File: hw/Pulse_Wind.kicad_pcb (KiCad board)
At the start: 2 copper layers, 0 parts

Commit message: hw: Layout & routing
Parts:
- added C1: 100n, Capacitor_SMD:C_0402_1005Metric, F.Cu at (85.8, 83.5)
- added C2: 100n, Capacitor_SMD:C_0402_1005Metric, F.Cu at (78.2, 80.3)
- added C3: 100n, Capacitor_SMD:C_0402_1005Metric, F.Cu at (84.2, 83.1)
- added C4: 1n, Capacitor_SMD:C_0402_1005Metric, F.Cu at (82.3, 85.0)
- added C5: 4.7u, Capacitor_SMD:C_0402_1005Metric, F.Cu at (83.8, 84.5)
- added C6: 4.7u, Capacitor_SMD:C_0402_1005Metric, F.Cu at (83.7, 93.4)
- added C91: 1u, Capacitor_SMD:C_0402_1005Metric, F.Cu at (78.2, 82.6)
- added C92: 1u, Capacitor_SMD:C_0402_1005Metric, F.Cu at (76.0, 80.2)
- added D1: LED_RAGB, LED_THT:LED_D5.0mm-4_RGB, B.Cu at (74.7, 89.8)
- added J1: AudioJack4, Connector_Audio:Jack_3.5mm_KoreanHropartsElec_PJ-320D-4A_Horizontal, B.Cu at (80.0, 80.0)
- added J2: Conn_01x04, TestPoints_P2.00:TestPoints_1x04_P2.00, F.Cu at (83.0, 77.1)
- added LS1: Speaker, Pulse_footprints:Pads_P2.00, B.Cu at (83.7, 90.8)
- added R1: 470, Resistor_SMD:R_0402_1005Metric, F.Cu at (74.8, 87.7)
- added R2: 470, Resistor_SMD:R_0402_1005Metric, F.Cu at (77.3, 87.7)
- added R3: 470, Resistor_SMD:R_0402_1005Metric, F.Cu at (78.5, 87.7)
- added R4: 100k, Resistor_SMD:R_0402_1005Metric, F.Cu at (82.3, 83.1)
- added R5: 22k, Resistor_SMD:R_0402_1005Metric, F.Cu at (82.3, 84.0)
- added U1: PY32F003F18U6, Package_DFN_QFN:QFN-20-1EP_3x3mm_P0.4mm_EP1.65x1.65mm, F.Cu at (84.2, 80.4)
- added U2: SC7A20, Package_LGA:LGA-12_2x2mm_P0.5mm, F.Cu at (80.0, 80.0)
- added U3: FM8002A, Package_SO:SOP-8_3.9x4.9mm_P1.27mm, F.Cu at (83.7, 89.2)
- added U9: ME6206A33XG, Package_TO_SOT_SMD:SOT-23, F.Cu at (76.0, 82.5)
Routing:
- net +3V3: track 0.00 -> 53.2 mm, vias 0 -> 2
- net /LED_R: track 0.00 -> 11.7 mm
- net Net-(U3-VO1): track 0.00 -> 9.07 mm, vias 0 -> 1
- net /LED_G: track 0.00 -> 8.84 mm
- net /LED_B: track 0.00 -> 8.72 mm
- net /ID_IN: track 0.00 -> 7.61 mm, vias 0 -> 1
- net /SWCLK: track 0.00 -> 5.20 mm
- net /SWDIO: track 0.00 -> 4.80 mm
- net VIN: track 0.00 -> 4.66 mm, vias 0 -> 1
- net Net-(U3-+IN): track 0.00 -> 3.62 mm
- net Net-(U3--IN): track 0.00 -> 3.52 mm
- net /IMU_SDA: track 0.00 -> 2.37 mm
- net /IMU_SCK: track 0.00 -> 2.31 mm
- net /IMU_CS: track 0.00 -> 2.07 mm
- net Net-(D1-GK): track 0.00 -> 1.65 mm
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- added copper zone on B.Cu, net GND
- added copper zone on F.Cu, net GND
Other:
- board outline added: 14 x 21 mm

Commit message: hw: Tweaks in the details
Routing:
- added copper zone on F.Cu, net +3V3
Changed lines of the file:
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@@
 	)
 	(segment
-		(start 86.386 83.556)
-		(end 86.386 85.264)
-		(width 0.25)
-		(layer "F.Cu")
-		(net 1)
-	)
-	(segment
-		(start 86.3 92.75)
-		(end 85.65 93.4)
+		(start 86.55 89.326131)
+		(end 86.55 92.8)
+		(width 0.25)
+		(layer "F.Cu")
+		(net 1)
+	)
+	(segment
+		(start 75.52 80.08)
+		(end 76.036 79.564)
+		(width 0.25)
+		(layer "F.Cu")
+		(net 1)
+	)
+	(segment
+		(start 85.885 82.97)
+		(end 86.386 83.471)
+		(width 0.25)
+		(layer "F.Cu")
+		(net 1)
+	)
+	(segment
+		(start 85.95 93.4)
+		(end 85.55 93.4)
 		(width 0.25)
 		(layer "F.Cu")
@@
 	)
 	(segment
+		(start 85.8 82.97)
+		(end 85.885 82.97)
+		(width 0.25)
+		(layer "F.Cu")
+		(net 1)
+	)
+	(segment
 		(start 79.95 78.574)
 		(end 79.75 78.774)
@@
 	)
 	(segment
+		(start 85.605 86.045)
+		(end 85.605 86.575)
+		(width 0.25)
+		(layer "F.Cu")
+		(net 1)
+	)
+	(segment
 		(start 83.17 93.4)
 		(end 82.4 93.4)
@@
 	)
 	(segment
-		(start 76.106 79.564)
-		(end 77.034 79.564)
-		(width 0.25)
-		(layer "F.Cu")
-		(net 1)
-	)
-	(segment
-		(start 85.65 93.4)
-		(end 85.55 93.4)
+		(start 86.55 92.8)
+		(end 85.95 93.4)
+		(width 0.25)
+		(layer "F.Cu")
+		(net 1)
+	)
+	(segment
+		(start 85.605 86.575)
+		(end 85.605 88.381131)
+		(width 0.25)
+		(layer "F.Cu")
+		(net 1)
+	)
+	(segment
+		(start 75.1 80.57)
+		(end 75.52 80.15)
+		(width 0.25)
+		(layer "F.Cu")
+		(net 1)
+	)
+	(segment
+		(start 73.55 91.6)
+		(end 74.982 91.6)
+		(width 0.25)
+		(layer "F.Cu")
+		(net 1)
+	)
+	(segment
+		(start 75.52 80.15)
+		(end 75.52 80.08)
+		(width 0.25)
+		(layer "F.Cu")
+		(net 1)
+	)
+	(segment
+		(start 86.386 83.471)
+		(end 86.386 85.264)
+		(width 0.25)
+		(layer "F.Cu")
+		(net 1)
+	)
+	(segment
+		(start 85.7 82.87)
+		(end 85.8 82.97)
+		(width 0.25)
+		(layer "F.Cu")
+		(net 1)
+	)
+	(segment
+		(start 82.8 93.4)
+		(end 76.782 93.4)
+		(width 0.25)
+		(layer "F.Cu")
+		(net 1)
+	)
+	(segment
+		(start 73.55 83.6)
+		(end 73.55 91.6)
+		(width 0.25)
+		(layer "F.Cu")
+		(net 1)
+	)
+	(segment
+		(start 79.75 79.2375)
+		(end 79.75 78.774)
+		(width 0.25)
+		(layer "F.Cu")
+		(net 1)
+	)
+	(segment
+		(start 78.25 80.78)
+		(end 79.2325 80.78)
+		(width 0.25)
+		(layer "F.Cu")
+		(net 1)
+	)
+	(segment
+		(start 77.034 79.564)
+		(end 78.25 80.78)
 		(width 0.25)
 		(layer "F.Cu")
@@
 	)
 	(segment
-		(start 86.3 89.076131)
-		(end 86.3 92.75)
-		(width 0.25)
-		(layer "F.Cu")
-		(net 1)
-	)
-	(segment
-		(start 75.1 80.57)
-		(end 75.52 80.15)
-		(width 0.25)
-		(layer "F.Cu")
-		(net 1)
-	)
-	(segment
-		(start 73.55 91.6)
-		(end 74.982 91.6)
-		(width 0.25)
-		(layer "F.Cu")
-		(net 1)
-	)
-	(segment
-		(start 85.7 82.87)
-		(end 85.8 82.97)
-		(width 0.25)
-		(layer "F.Cu")
-		(net 1)
-	)
-	(segment
-		(start 82.8 93.4)
-		(end 76.782 93.4)
-		(width 0.25)
-		(layer "F.Cu")
-		(net 1)
-	)
-	(segment
-		(start 73.55 83.6)
-		(end 73.55 91.6)
-		(width 0.25)
-		(layer "F.Cu")
-		(net 1)
-	)
-	(segment
-		(start 75.52 80.15)
-		(end 76.106 79.564)
-		(width 0.25)
-		(layer "F.Cu")
-		(net 1)
-	)
-	(segment
-		(start 79.75 79.2375)
-		(end 79.75 78.774)
-		(width 0.25)
-		(layer "F.Cu")
-		(net 1)
-	)
-	(segment
-		(start 78.25 80.78)
-		(end 79.2325 80.78)
-		(width 0.25)
-		(layer "F.Cu")
-		(net 1)
-	)
-	(segment
-		(start 77.034 79.564)
-		(end 78.25 80.78)
-		(width 0.25)
-		(layer "F.Cu")
-		(net 1)
-	)
-	(segment
 		(start 79.95 77.1)
 		(end 79.95 78.574)
@@
 	)
 	(segment
+		(start 76.036 79.564)
+		(end 77.034 79.564)
+		(width 0.25)
+		(layer "F.Cu")
+		(net 1)
+	)
+	(segment
+		(start 85.605 88.381131)
+		(end 86.55 89.326131)
+		(width 0.25)
+		(layer "F.Cu")
+		(net 1)
+	)
+	(segment
 		(start 79.2325 80.78)
 		(end 79.25 80.7625)
@@
 	)
 	(segment
-		(start 85.8 82.97)
-		(end 86.386 83.556)
-		(width 0.25)
-		(layer "F.Cu")
-		(net 1)
-	)
-	(segment
-		(start 85.605 86.575)
-		(end 85.605 88.381131)
-		(width 0.25)
-		(layer "F.Cu")
-		(net 1)
-	)
-	(segment
 		(start 75.1 81.6125)
 		(end 75.1 80.57)
@@
 	)
 	(segment
-		(start 85.605 86.045)
-		(end 85.605 86.575)
-		(width 0.25)
-		(layer "F.Cu")
-		(net 1)
-	)
-	(segment
 		(start 75.1 82.05)
 		(end 73.55 83.6)
@@
 	)
 	(segment
-		(start 85.605 88.381131)
-		(end 86.3 89.076131)
-		(width 0.25)
-		(layer "F.Cu")
-		(net 1)
-	)
-	(segment
 		(start 79.75 78.774)
 		(end 77.824 78.774)
@@
 	)
 	(segment
-		(start 81.85 79.6)
+		(start 80.75 78.55)
+		(end 81.8 79.6)
+		(width 0.15)
+		(layer "F.Cu")
+		(net 13)
+	)
+	(segment
+		(start 80.55 78.55)
+		(end 80.75 78.55)
+		(width 0.15)
+		(layer "F.Cu")
+		(net 13)
+	)
+	(segment
+		(start 81.8 79.6)
 		(end 82.8 79.6)
-		(width 0.15)
-		(layer "F.Cu")
-		(net 13)
-	)
-	(segment
-		(start 80.8 78.55)
-		(end 81.85 79.6)
-		(width 0.15)
-		(layer "F.Cu")
-		(net 13)
-	)
-	(segment
-		(start 80.55 78.55)
-		(end 80.8 78.55)
 		(width 0.15)
 		(layer "F.Cu")
@@
 	)
 	(segment
+		(start 82.1 82.501)
+		(end 83.624 82.501)
+		(width 0.15)
+		(layer "F.Cu")
+		(net 19)
+	)
+	(segment
 		(start 81.604726 82.501)
-		(end 83.624 82.501)
+		(end 82.1 82.501)
 		(width 0.15)
 		(layer "F.Cu")
@@
 	)
 	(segment
+		(start 81.6 80.4)
+		(end 82.8 80.4)
+		(width 0.15)
+		(layer "F.Cu")
+		(net 24)
+	)
+	(segment
 		(start 80.7625 79.75)
-		(end 81.104914 79.75)
+		(end 80.95 79.75)
 		(width 0.15)
 		(layer "F.Cu")
@@
 	)
 	(segment
-		(start 81.754914 80.4)
-		(end 82.8 80.4)
-		(width 0.15)
-		(layer "F.Cu")
-		(net 24)
-	)
-	(segment
-		(start 81.104914 79.75)
-		(end 81.754914 80.4)
+		(start 80.95 79.75)
+		(end 81.6 80.4)
 		(width 0.15)
 		(layer "F.Cu")
@@
 	)
 	(segment
+		(start 80.9375 79.2375)
+		(end 81.7 80)
+		(width 0.15)
+		(layer "F.Cu")
+		(net 26)
+	)
+	(segment
 		(start 80.75 79.2375)
-		(end 81.0375 79.2375)
+		(end 80.9375 79.2375)
 		(width 0.15)
 		(layer "F.Cu")
@@
 	)
 	(segment
-		(start 81.8 80)
+		(start 81.7 80)
 		(end 82.8 80)
 		(width 0.15)
@@
 		(net 26)
 	)
-	(segment
-		(start 81.0375 79.2375)
-		(end 81.8 80)
-		(width 0.15)
-		(layer "F.Cu")
-		(net 26)
+	(zone
+		(net 1)
+		(net_name "+3V3")
+		(layer "F.Cu")
+		(hatch edge 0.5)
+		(priority 1)
+		(connect_pads yes
+			(clearance 0.15)
+		)
+		(min_thickness 0.15)
+		(filled_areas_thickness no)
+		(fill yes
+			(thermal_gap 0.5)
+			(thermal_bridge_width 0.5)
+		)
+		(polygon
+			(pts
+				(xy 77.25 79.3) (xy 76.85 79.6) (xy 77.25 79.85)
+			)
+		)
 	)
 	(zone
@@
 	(group ""
 		(members "0a00f7a9-fa76-4db4-9a4f-3405817b9888" "0c27577c-8093-4abf-b581-fb53b4ebbdfd"
-			"126b8e08-2343-439d-9c2f-2fc3c2823dc1" "190c0173-98dd-427d-8aaf-91ffee57b51c"
-			"1a010d36-e23c-4886-b763-da91e41b8a25" "20fa108a-531c-433f-8208-e388e762526e"
-			"23740dcb-cfe1-4826-8513-a80f5515eafc" "2b0f7574-dd0b-4eaa-a151-ab3c0bf23453"
-			"2ee08ae1-401a-4be4-928a-3aa71db18f79" "319b7428-eb06-433f-97d2-fd98b86ea2a8"
+			"126b8e08-2343-439d-9c2f-2fc3c2823dc1" "14e91b02-dc97-4663-a828-29cd680795b5"
+			"190c0173-98dd-427d-8aaf-91ffee57b51c" "1a010d36-e23c-4886-b763-da91e41b8a25"
+			"20fa108a-531c-433f-8208-e388e762526e" "286e7929-e18a-4375-b21d-e89e9923bf50"
+			"2b0f7574-dd0b-4eaa-a151-ab3c0bf23453" "2ee08ae1-401a-4be4-928a-3aa71db18f79"
 			"33f61983-a144-4bfd-a546-e691e0ed24ae" "47488a29-3616-4fd2-b05c-483a48057a60"
 			"48116a51-740d-4dbc-a903-da079f2910ff" "4bcaf329-5988-400e-b6d2-94e9bc71c217"
-			"504d98e9-751c-48b7-bf62-39e115cf3ae9" "520691c8-52d3-4ed5-b961-be06734bc9a1"
-			"521af52b-4c40-4755-929e-333bd30f994a" "5e25deb0-4ced-4fcb-9a0c-ce8415f39fb9"
-			"61b3d5b3-a7f9-4d20-8404-9289bef1dcf6" "6c950410-fae0-447f-b75f-f7ef918c0d24"
+			"504d98e9-751c-48b7-bf62-39e115cf3ae9" "5119c6e3-4941-4b9e-8f9f-909a5a979d35"
+			"520691c8-52d3-4ed5-b961-be06734bc9a1" "521af52b-4c40-4755-929e-333bd30f994a"
+			"61b3d5b3-a7f9-4d20-8404-9289bef1dcf6" "6b151099-a487-4f2e-85b7-a3b44b115259"
 			"73a8a405-c205-4d5c-abf3-10ea13343f63" "78f7f928-7258-46a6-932a-0e27c65096c3"
 			"8e6700c2-dadd-4a54-82e3-83281ae790e7" "96d62d3e-b6f2-4224-b957-0242920720d7"
@@
 			"e2612b23-cf4d-4c01-aef6-73e01c965712" "e6a01eb8-74b0-4068-b2c5-711ac98a3915"
 			"e8fa09f2-a721-42c8-817e-22138d5fde34" "ed2f3910-88e6-42a0-935b-fe5d44aa59d2"
-			"ee9c342a-25c3-4af7-ab8f-9c9d59d5d2b7" "f094dbaa-ec3d-4aee-afec-00c7b9ee9c13"
-			"f1b3a12f-37f9-43ca-b6f2-0da495f89518" "fb245c76-abd6-4ef4-a7bd-30e3b97d6cda"
+			"f094dbaa-ec3d-4aee-afec-00c7b9ee9c13" "f1b3a12f-37f9-43ca-b6f2-0da495f89518"
 		)
 	)

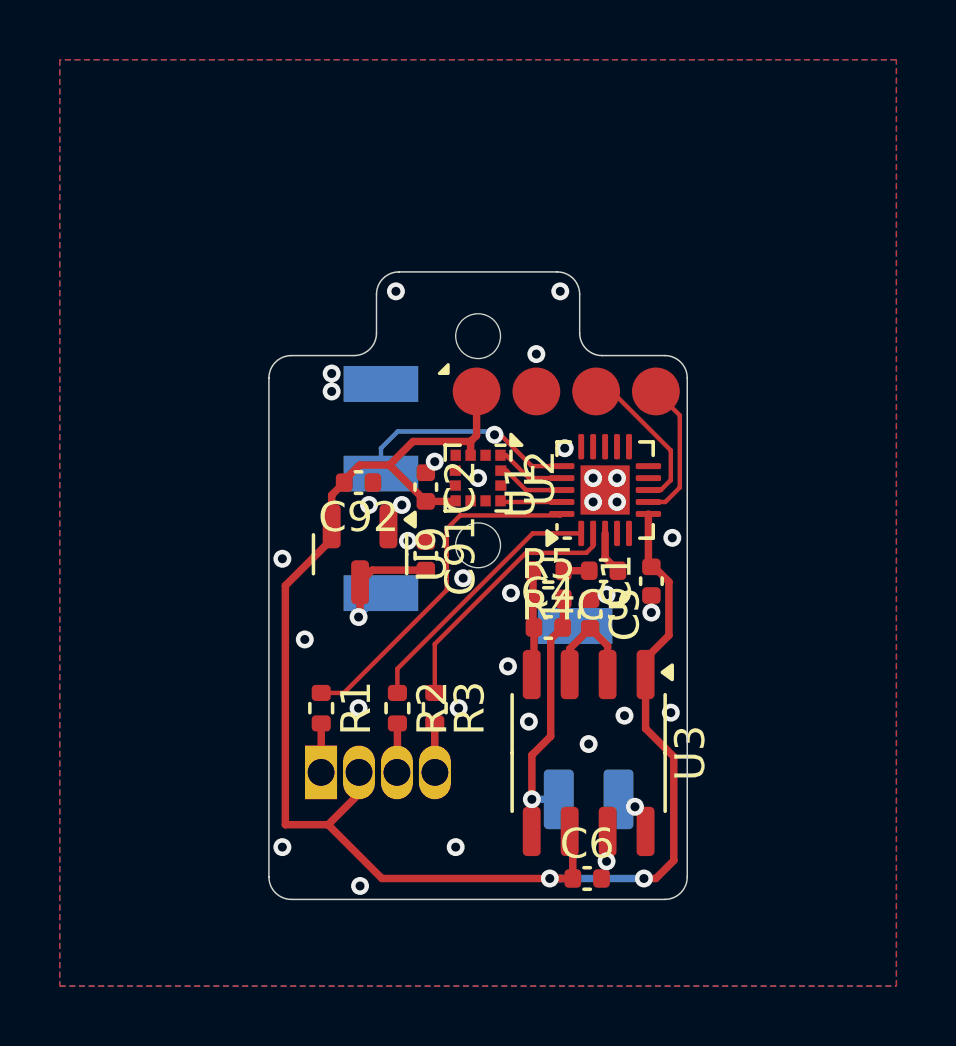
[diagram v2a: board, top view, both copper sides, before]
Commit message: hw: Adjust silkscreen
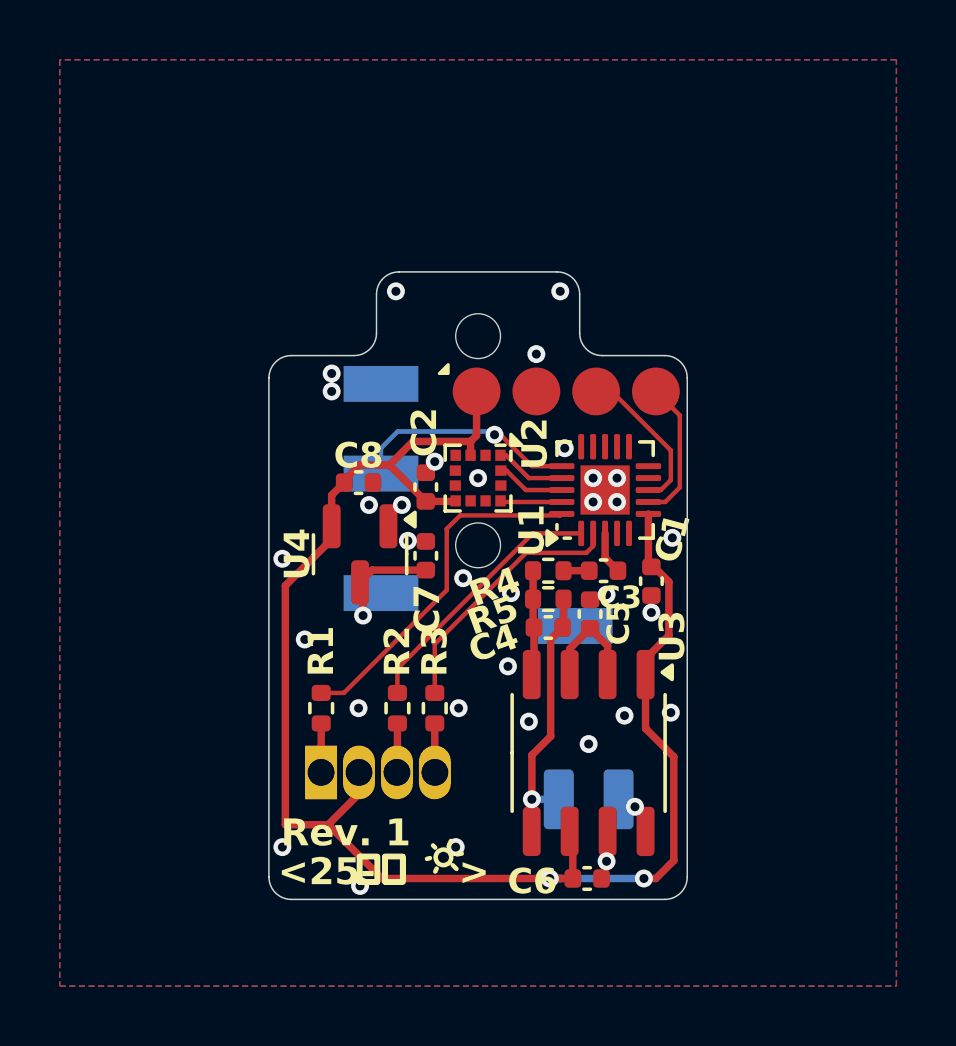
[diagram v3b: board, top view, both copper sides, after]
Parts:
- added G***: LOGO, LOGO, B.Cu at (85.0, 78.6)
- renumbered C91 to C7, C92 to C8, U9 to U4
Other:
- board text added: "<25-"
- board text added: ">"
- board text added: "JLCJLCJLCJLC"
- board text added: "Rev. 1"
- board text added: "大暑"
